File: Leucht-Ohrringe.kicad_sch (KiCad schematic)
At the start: 29 parts, among them J1 Conn_ARM_SWD_TagConnect_TC2030, P1 USB_C_Plug_USB2.0, SW1 SW_SPDT, U1 TX4204, U3 ICM-42670-L, U4 CH340N, U5 nRF52832-QFxx

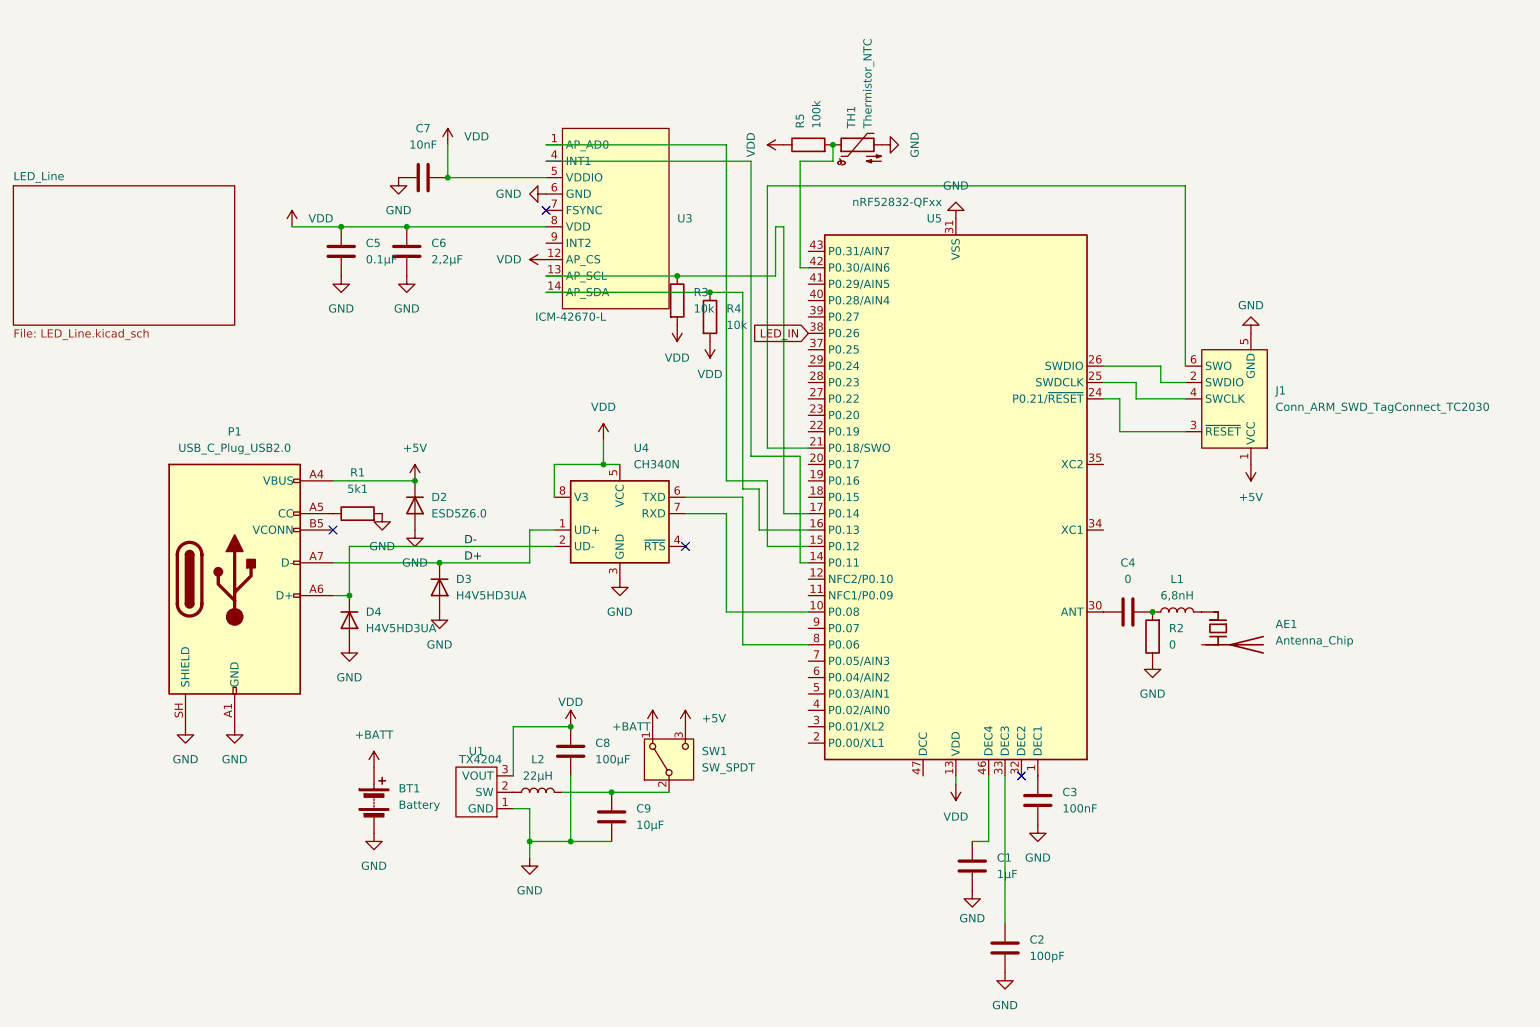
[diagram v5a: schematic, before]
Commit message: fix CH340N, add pads for gpios, add switch model
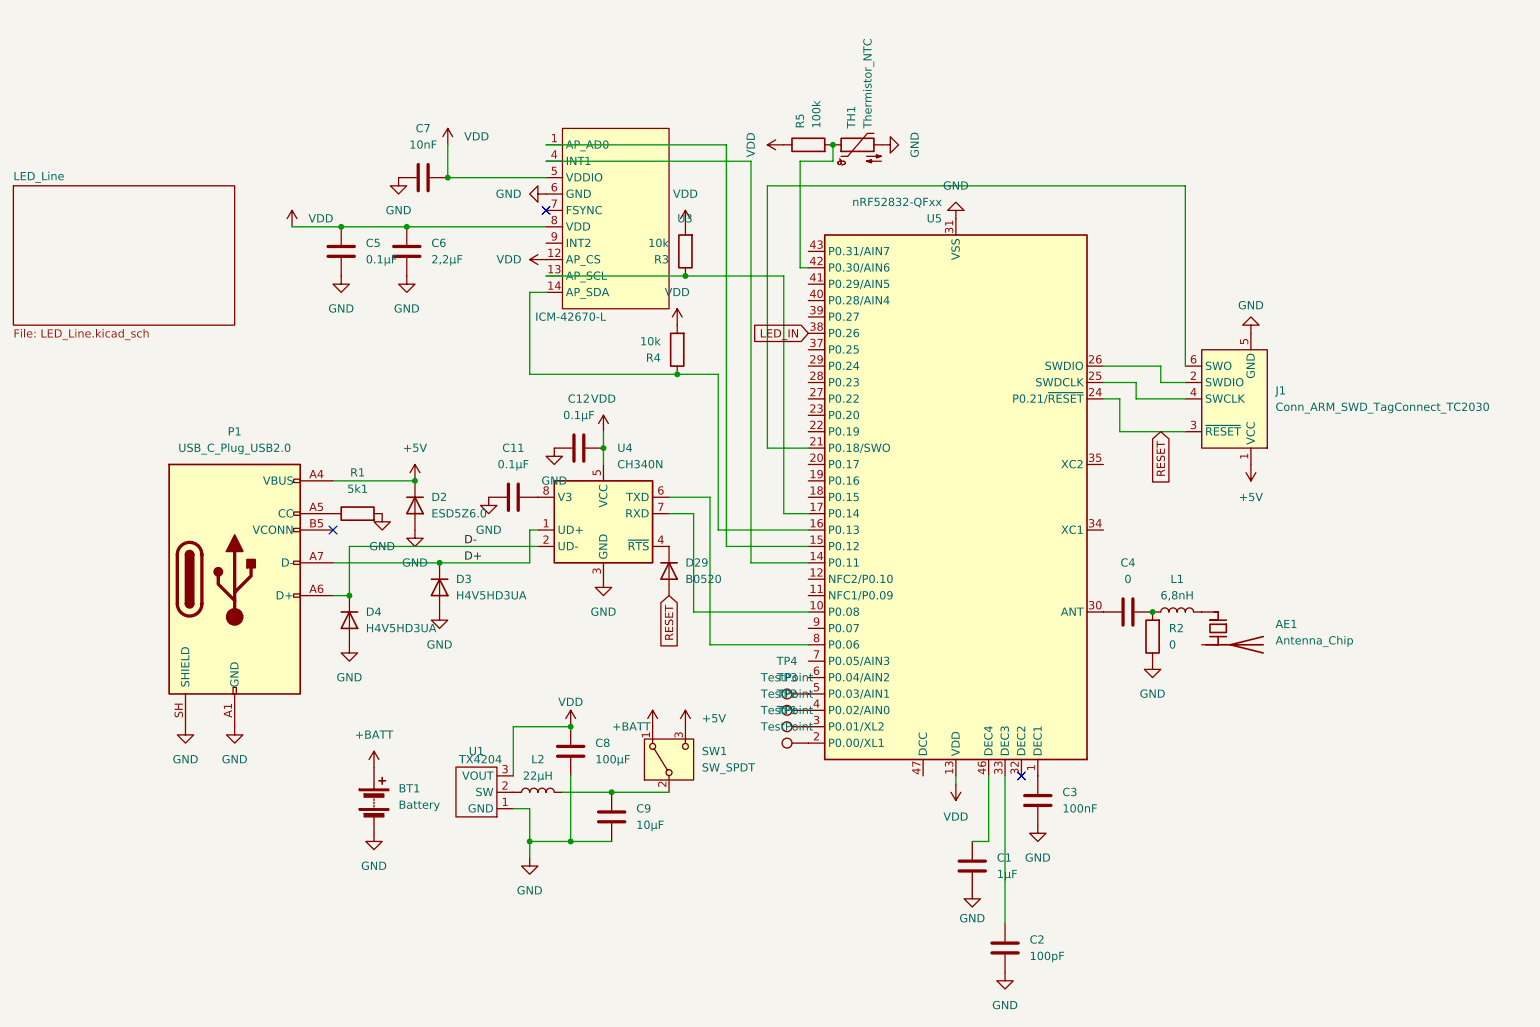
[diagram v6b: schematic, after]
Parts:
- added C11, C12: 0.1µF, Capacitor_SMD:C_0402_1005Metric_Pad0.74x0.62mm_HandSolder, symbol Device:C
- added D29: B0520, Diode_SMD:D_SOD-523, symbol Device:D
- added TP1, TP2, TP3, TP4: TestPoint, Inductor_SMD:TestPoint_0,5mm, symbol Connector:TestPoint
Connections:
- net GND: now also C11.2, C12.2
- net VDD: now also C12.1; no longer U4.8 (V3)
- net RESET: now reaches J1.3 (~{RESET}), U5.24 (P0.21/~{RESET})
- net RESET: now also D29.2 (A)
- net at U5.2 (P0.00/XL1): now also TP1.1
- net at U5.3 (P0.01/XL2): now also TP2.1
- net at U5.4 (P0.02/AIN0): now also TP3.1
- net at U5.5 (P0.03/AIN1): now also TP4.1
- net at U4.4 (~{RTS}): now also D29.1 (K)
- new net: C11.1, U4.8 (V3)
- no-connect marks 4 -> 3
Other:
- moved on the sheet: R3, R4, U4

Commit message: update fab
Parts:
- C8: LCSC C380356 -> C15008
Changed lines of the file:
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@@
 			)
 		)
-		(property "LCSC" "C380356"
+		(property "LCSC" "C15008"
 			(at 107.95 111.76 0)
 			(hide yes)

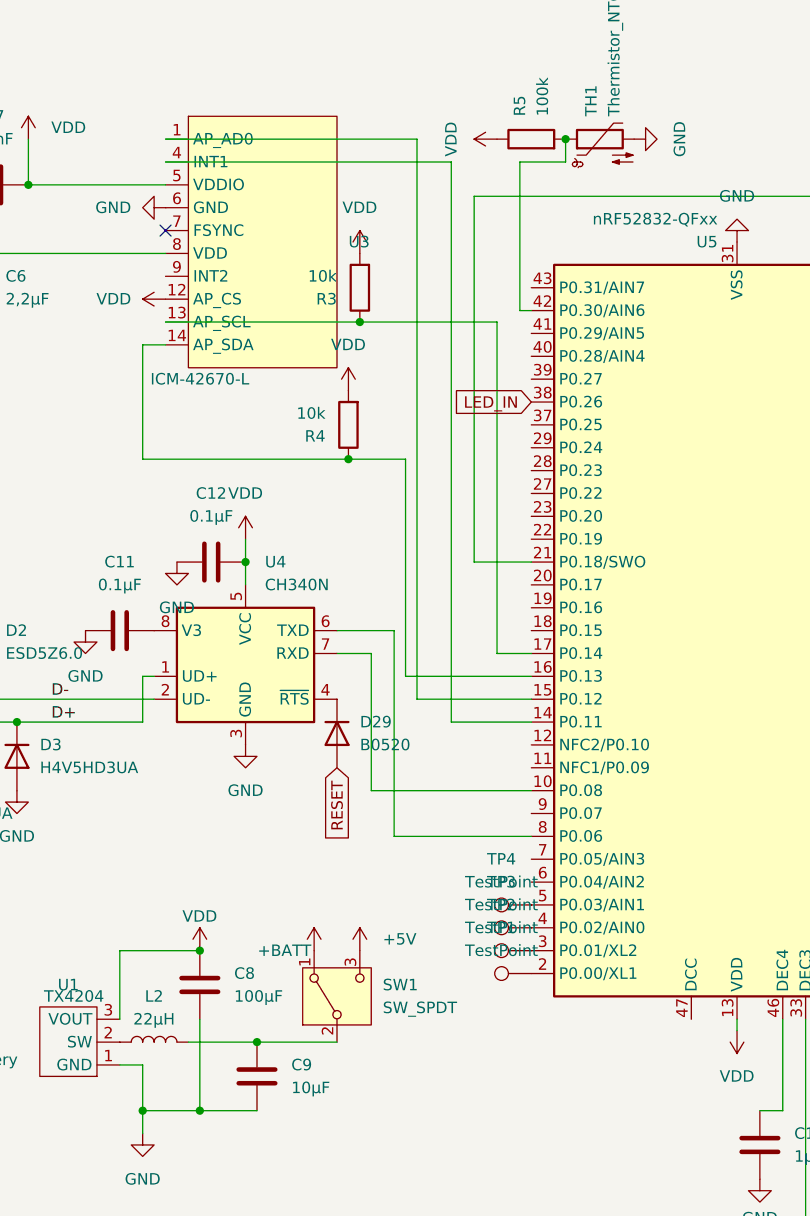
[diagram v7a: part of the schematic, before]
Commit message: add gpio pads, change to jst sh 1mm
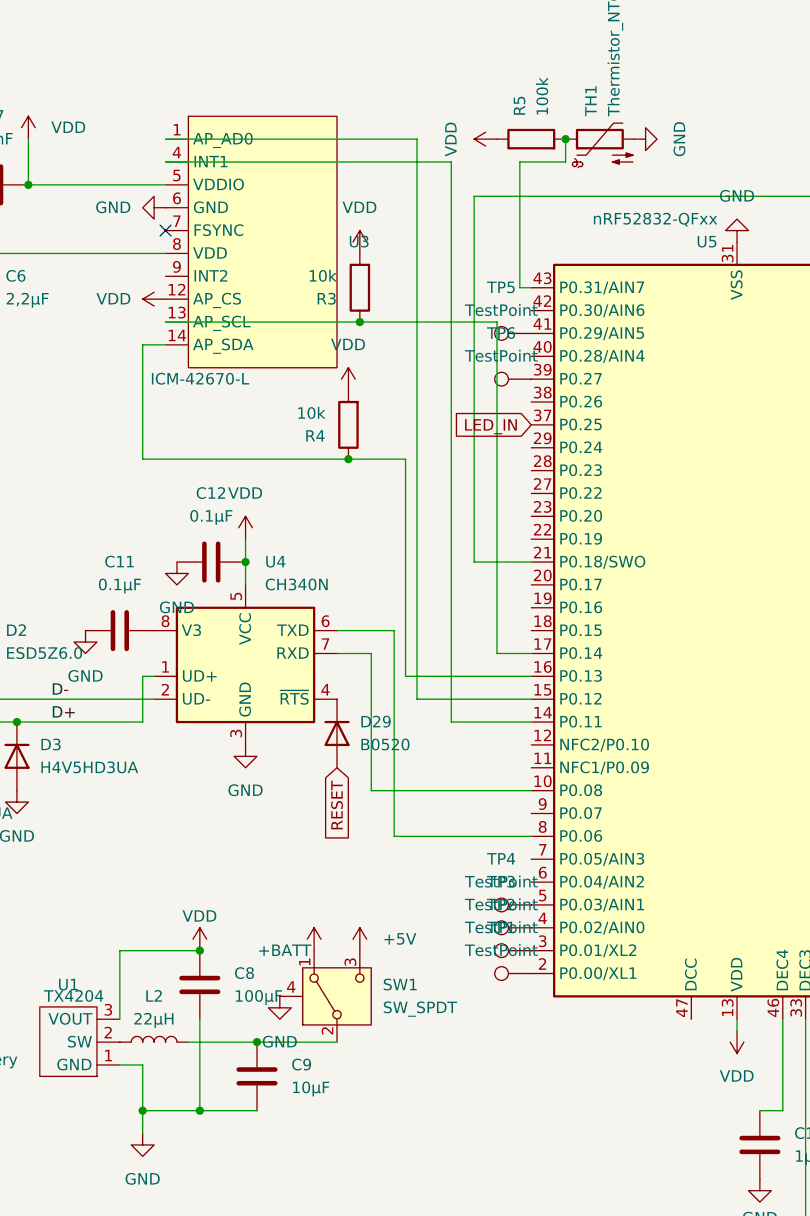
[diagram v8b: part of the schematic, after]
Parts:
- added TP5, TP6: TestPoint, Inductor_SMD:TestPoint_0,5mm, symbol Connector:TestPoint
- BT1: footprint Connector_JST:JST_GH_SM02B-GHS-TB_1x02-1MP_P1.25mm_Horizontal -> Connector_JST:JST_SH_SM02B-SRSS-TB_1x02-1MP_P1.00mm_Horizontal
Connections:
- net GND: now also SW1.4 (SHIELD)
- net LED_IN: now also U5.37 (P0.25); no longer U5.38 (P0.26)
- net at R5.2, TH1.1: now also U5.43 (P0.31/AIN7); no longer U5.42 (P0.30/AIN6)
- net at U5.39 (P0.27): now also TP6.1
- net at U5.41 (P0.29/AIN5): now also TP5.1
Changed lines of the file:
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@@
 	(wire
 		(pts
-			(xy 143.51 36.83) (xy 144.78 36.83)
+			(xy 104.14 20.32) (xy 135.89 20.32)
 		)
 		(stroke
@@
 	(wire
 		(pts
-			(xy 104.14 20.32) (xy 135.89 20.32)
+			(xy 135.89 82.55) (xy 144.78 82.55)
 		)
 		(stroke
@@
 	(wire
 		(pts
-			(xy 135.89 82.55) (xy 144.78 82.55)
+			(xy 132.08 80.01) (xy 144.78 80.01)
 		)
 		(stroke
@@
 	(wire
 		(pts
-			(xy 132.08 80.01) (xy 144.78 80.01)
+			(xy 143.51 20.32) (xy 143.51 34.29)
 		)
 		(stroke
@@
 	(wire
 		(pts
+			(xy 143.51 34.29) (xy 144.78 34.29)
+		)
+		(stroke
+			(width 0)
+			(type default)
+		)
+	)
+	(wire
+		(pts
 			(xy 104.14 38.1) (xy 125.73 38.1)
 		)
@@
 		)
 	)
-	(wire
-		(pts
-			(xy 143.51 20.32) (xy 143.51 36.83)
-		)
-		(stroke
-			(width 0)
-			(type default)
-		)
-	)
 	(label "D+"
 		(at 91.44 82.55 0)
@@
 		)
 	)
-	(global_label "RESET"
+	(global_label "LED_IN"
 		(shape input)
-		(at 123.19 87.63 270)
+		(at 144.78 49.53 180)
 		(fields_autoplaced yes)
 		(effects
@@
 		)
 		(property "Intersheetrefs" "${INTERSHEET_REFS}"
-			(at 123.19 96.3603 90)
+			(at 135.4448 49.53 0)
 			(hide yes)
 			(show_name no)
@@
 	(global_label "RESET"
 		(shape input)
-		(at 199.39 62.23 270)
+		(at 123.19 87.63 270)
 		(fields_autoplaced yes)
 		(effects
@@
 		)
 		(property "Intersheetrefs" "${INTERSHEET_REFS}"
-			(at 199.39 70.9603 90)
+			(at 123.19 96.3603 90)
 			(hide yes)
 			(show_name no)
@@
 		)
 	)
-	(global_label "LED_IN"
+	(global_label "RESET"
 		(shape input)
-		(at 144.78 46.99 180)
+		(at 199.39 62.23 270)
 		(fields_autoplaced yes)
 		(effects
@@
 		)
 		(property "Intersheetrefs" "${INTERSHEET_REFS}"
-			(at 135.4448 46.99 0)
+			(at 199.39 70.9603 90)
 			(hide yes)
 			(show_name no)
@@
 		(pin "3"
 		)
+		(pin "4"
+		)
 		(instances
 			(project "Leucht-Ohrringe"
@@
 	)
 	(symbol
+		(lib_id "power:GND")
+		(at 116.84 113.03 0)
+		(unit 1)
+		(body_style 1)
+		(exclude_from_sim no)
+		(in_bom yes)
+		(on_board yes)
+		(in_pos_files yes)
+		(dnp no)
+		(fields_autoplaced yes)
+		(property "Reference" "#PWR089"
+			(at 116.84 119.38 0)
+			(hide yes)
+			(show_name no)
+			(do_not_autoplace no)
+			(effects
+				(font
+					(size 1.27 1.27)
+				)
+			)
+		)
+		(property "Value" "GND"
+			(at 116.84 118.11 0)
+			(show_name no)
+			(do_not_autoplace no)
+			(effects
+				(font
+					(size 1.27 1.27)
+				)
+			)
+		)
+		(property "Footprint" ""
+			(at 116.84 113.03 0)
+			(hide yes)
+			(show_name no)
+			(do_not_autoplace no)
+			(effects
+				(font
+					(size 1.27 1.27)
+				)
+			)
+		)
+		(property "Datasheet" ""
+			(at 116.84 113.03 0)
+			(hide yes)
+			(show_name no)
+			(do_not_autoplace no)
+			(effects
+				(font
+					(size 1.27 1.27)
+				)
+			)
+		)
+		(property "Description" "Power symbol creates a global label with name \"GND\" , ground"
+			(at 116.84 113.03 0)
+			(hide yes)
+			(show_name no)
+			(do_not_autoplace no)
+			(effects
+				(font
+					(size 1.27 1.27)
+				)
+			)
+		)
+		(pin "1"
+		)
+		(instances
+			(project "Leucht-Ohrringe"
+				(path "/4432a709-2b65-441b-8d8c-961e244b0ba3"
+					(reference "#PWR089")
+					(unit 1)
+				)
+			)
+		)
+	)
+	(symbol
 		(lib_id "Device:C")
 		(at 82.55 34.29 0)
@@
 	)
 	(symbol
+		(lib_id "Connector:TestPoint")
+		(at 144.78 44.45 90)
+		(unit 1)
+		(body_style 1)
+		(exclude_from_sim no)
+		(in_bom yes)
+		(on_board yes)
+		(in_pos_files yes)
+		(dnp no)
+		(fields_autoplaced yes)
+		(property "Reference" "TP6"
+			(at 141.478 39.37 90)
+			(show_name no)
+			(do_not_autoplace no)
+			(effects
+				(font
+					(size 1.27 1.27)
+				)
+			)
+		)
+		(property "Value" "TestPoint"
+			(at 141.478 41.91 90)
+			(show_name no)
+			(do_not_autoplace no)
+			(effects
+				(font
+					(size 1.27 1.27)
+				)
+			)
+		)
+		(property "Footprint" "Inductor_SMD:TestPoint_0,5mm"
+			(at 144.78 39.37 0)
+			(hide yes)
+			(show_name no)
+			(do_not_autoplace no)
+			(effects
+				(font
+					(size 1.27 1.27)
+				)
+			)
+		)
+		(property "Datasheet" ""
+			(at 144.78 39.37 0)
+			(hide yes)
+			(show_name no)
+			(do_not_autoplace no)
+			(effects
+				(font
+					(size 1.27 1.27)
+				)
+			)
+		)
+		(property "Description" "test point"
+			(at 144.78 44.45 0)
+			(hide yes)
+			(show_name no)
+			(do_not_autoplace no)
+			(effects
+				(font
+					(size 1.27 1.27)
+				)
+			)
+		)
+		(pin "1"
+		)
+		(instances
+			(project "Leucht-Ohrringe"
+				(path "/4432a709-2b65-441b-8d8c-961e244b0ba3"
+					(reference "TP6")
+					(unit 1)
+				)
+			)
+		)
+	)
+	(symbol
 		(lib_id "Device:C")
 		(at 194.31 90.17 90)
@@
 			)
 		)
-		(property "Footprint" "Connector_JST:JST_GH_SM02B-GHS-TB_1x02-1MP_P1.25mm_Horizontal"
+		(property "Footprint" "Connector_JST:JST_SH_SM02B-SRSS-TB_1x02-1MP_P1.00mm_Horizontal"
 			(at 77.47 117.856 90)
 			(hide yes)
@@
 					(unit 1)
 				)
+			)
+		)
+	)
+	(symbol
+		(lib_id "Connector:TestPoint")
+		(at 144.78 39.37 90)
+		(unit 1)
+		(body_style 1)
+		(exclude_from_sim no)
+		(in_bom yes)
+		(on_board yes)
+		(in_pos_files yes)
+		(dnp no)
+		(fields_autoplaced yes)
+		(property "Reference" "TP5"
+			(at 141.478 34.29 90)
+			(show_name no)
+			(do_not_autoplace no)
+			(effects
+				(font
+					(size 1.27 1.27)
+				)
+			)
+		)
+		(property "Value" "TestPoint"
+			(at 141.478 36.83 90)
+			(show_name no)
+			(do_not_autoplace no)
+			(effects
+				(font
+					(size 1.27 1.27)
+				)
+			)
+		)
+		(property "Footprint" "Inductor_SMD:TestPoint_0,5mm"
+			(at 144.78 34.29 0)
+			(hide yes)
+			(show_name no)
+			(do_not_autoplace no)
+			(effects
+				(font
+					(size 1.27 1.27)
+				)
+			)
+		)
+		(property "Datasheet" ""
+			(at 144.78 34.29 0)
+			(hide yes)
+			(show_name no)
+			(do_not_autoplace no)
+			(effects
+				(font
+					(size 1.27 1.27)
+				)
+			)
+		)
+		(property "Description" "test point"
+			(at 144.78 39.37 0)
+			(hide yes)
+			(show_name no)
+			(do_not_autoplace no)
+			(effects
+				(font
+					(size 1.27 1.27)
+				)
+			)
+		)
+		(pin "1"
+		)
+		(instances
+			(project "Leucht-Ohrringe"
+				(path "/4432a709-2b65-441b-8d8c-961e244b0ba3"
+					(reference "TP5")
+					(unit 1)
+				)
